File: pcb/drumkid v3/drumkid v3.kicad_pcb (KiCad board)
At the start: 2 copper layers, 90 x 120 mm, 61 parts, among them J1 Conn_01x04_Female, J5 Conn_01x05_Female, J6 Conn_01x04_Female, J7 Conn_01x06_Female, J8 Conn_01x05_Female, J9 AudioJack3_Ground_Switch, SW1 SW_SPDT, SW2 SW_Push, SW3 SW_Push, SW4 SW_Push, SW5 SW_Push, SW6 SW_Push, SW7 SW_Push, U2 ATmega328P-PU, U3 LM386, Y1 Crystal

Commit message: pcb layout looking nice (v3)
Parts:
- moved C16 16.9 mm to (167.7, 130.8)
- moved R8 10.4 mm to (142.2, 124.6), turned to 90 degrees
- moved R9 9.22 mm to (137.2, 124.6), turned to 90 degrees
- moved R1 8.99 mm to (139.7, 124.6), turned to 90 degrees
- moved R2 7.71 mm to (174.0, 133.3)
- moved R7 5.28 mm to (174.0, 130.8)
- moved R6 4.83 mm to (174.0, 128.3)
- moved U2 4.74 mm to (172.7, 139.7)
- moved R5 4.38 mm to (174.0, 125.7)
- moved R4 3.93 mm to (174.0, 123.2)
- moved R3 3.49 mm to (174.0, 120.7)
- moved J1 3.43 mm to (125.7, 146.1)
- moved C14 2.36 mm to (128.3, 134.6)
- moved C18 2.29 mm to (167.6, 125.7)
- moved C15 2.28 mm to (128.3, 118.1)
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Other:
- board text added: "5V 5V GND GND"
- board text added: "D4 D3 D2 D1 D0 A5 A4 A3 A2 A1 A0"
- board text added: "D5 D6 D7 D8 D9 D10 D11 D12 D13"

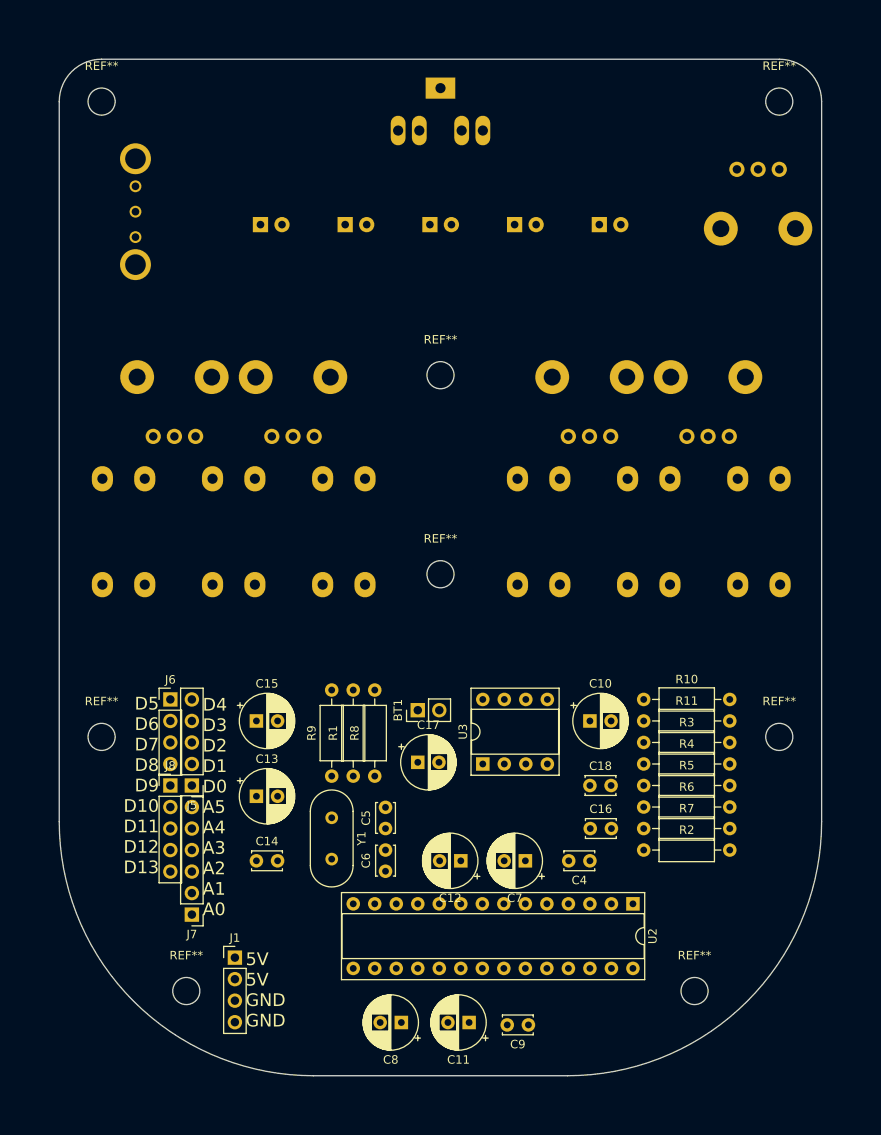
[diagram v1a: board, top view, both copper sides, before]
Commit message: silkscreen layers looking decent
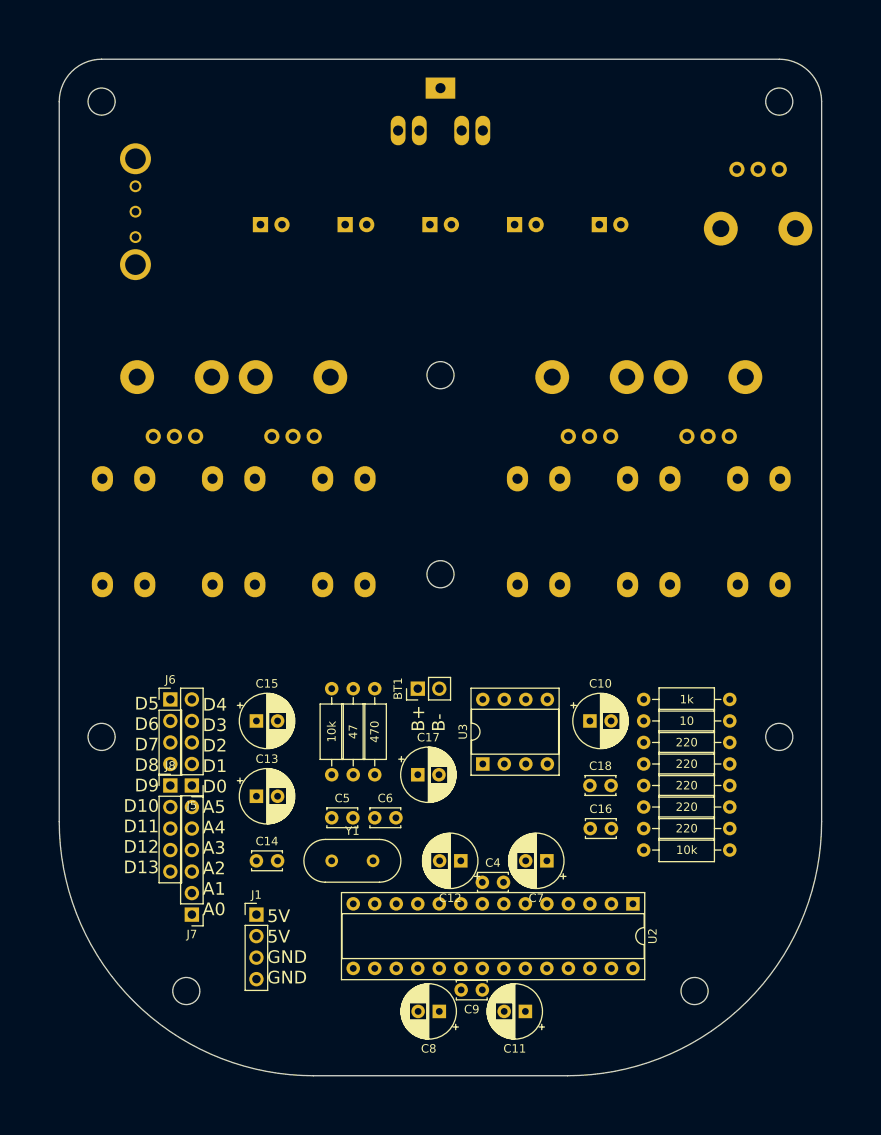
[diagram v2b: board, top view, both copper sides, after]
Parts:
- D2, D3, D4, D5, D6: footprint LED_THT:LED_D5.0mm -> headphone:LED_D5.0mm_NOSILK
- J9: footprint headphone:Tayda_3.5mm_stereo_TRS_jack_A-853 -> headphone:Tayda_3.5mm_stereo_TRS_jack_A-853_NOSILK
- R1, R10, R11, R2, R3, R4, R5, R6, R7, R8, R9: footprint Resistor_THT:R_Axial_DIN0207_L6.3mm_D2.5mm_P10.16mm_Horizontal -> headphone:R_Axial_DIN0207_L6.3mm_D2.5mm_P10.16mm_Horizontal_VALMOD
- RV1, RV2, RV3, RV4, RV5: footprint Potentiometer_THT:Potentiometer_Alps_RK09K_Single_Vertical -> headphone:Potentiometer_Alps_RK09K_Single_Vertical_NOSILK
- SW1: footprint SamacSys_Parts:EG1206 -> headphone:EG1206_NOSILK
- SW2, SW3, SW4, SW5, SW6, SW7: footprint Button_Switch_THT:SW_PUSH-12mm_Wuerth-430476085716 -> headphone:SW_PUSH-12mm_Wuerth-430476085716_NOSILK
- moved C4 13.0 mm to (154.9, 137.2), turned to 0 degrees
- moved C9 6.83 mm to (154.9, 149.9)
- moved C11 6.77 mm to (160.0, 152.4)
- moved C5 6.48 mm to (137.2, 129.5), turned to 0 degrees
- moved C6 6.44 mm to (142.2, 129.5), turned to 0 degrees
- moved J1 5.68 mm to (128.3, 141.0)
- moved Y1 5.08 mm to (137.2, 134.6), turned to 0 degrees
- moved C8 4.67 mm to (149.9, 152.4)
- moved BT1 2.54 mm to (147.3, 114.3)
- moved C7 2.54 mm to (162.6, 134.6)
- moved C17 1.47 mm to (147.3, 124.5)
- moved R1 0.16 mm to (139.7, 124.5)
- moved R8 0.16 mm to (142.2, 124.5)
- moved R9 0.16 mm to (137.2, 124.5)
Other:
- board text added: "B+ B-"

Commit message: half way through routing
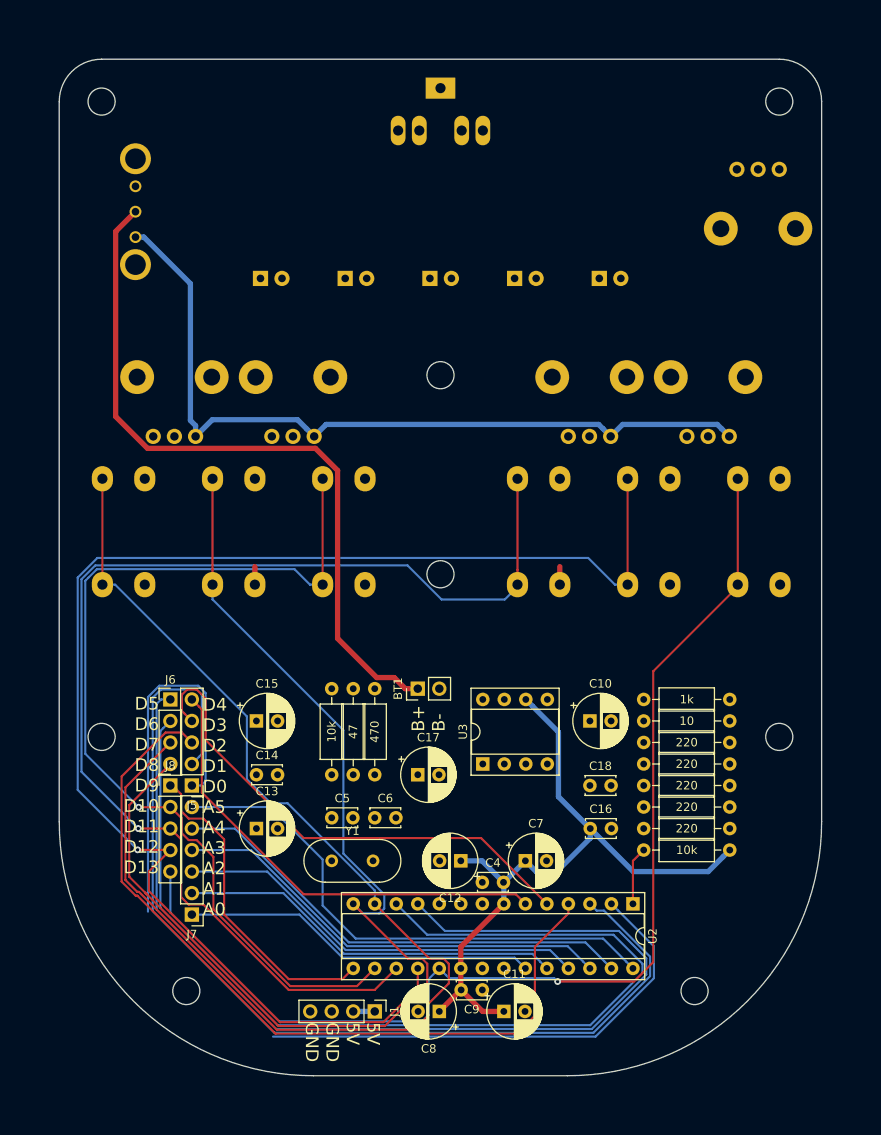
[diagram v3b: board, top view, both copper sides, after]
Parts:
- moved J1 18.1 mm to (142.2, 152.4), turned to 270 degrees
- moved C14 10.2 mm to (128.3, 124.5)
- moved D2 6.35 mm to (128.8, 65.9)
- moved D3 6.35 mm to (138.8, 65.9)
- moved D4 6.35 mm to (148.8, 65.9)
- moved D5 6.35 mm to (158.8, 65.9)
- moved D6 6.35 mm to (168.8, 65.9)
- moved C13 3.81 mm to (128.3, 130.8)
- moved C11 2.54 mm to (157.5, 152.4), turned to 0 degrees
- moved C7 2.54 mm to (160.0, 134.6), turned to 0 degrees
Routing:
- net +5V: track 0.00 -> 179.9 mm
- net /DIGITAL_12: track 0.00 -> 166.6 mm, vias 0 -> 1
- net /DIGITAL_7: track 0.00 -> 146.5 mm
- net /DIGITAL_11: track 0.00 -> 142.8 mm, vias 0 -> 1
- net /DIGITAL_8: track 0.00 -> 137.7 mm
- net /DIGITAL_13: track 0.00 -> 135.0 mm, vias 0 -> 1
- net /DIGITAL_5: track 0.00 -> 124.0 mm
- net /DIGITAL_6: track 0.00 -> 120.8 mm
- net /DIGITAL_1: track 0.00 -> 119.7 mm
- net /DIGITAL_10: track 0.00 -> 113.3 mm, vias 0 -> 1
- net /DIGITAL_0: track 0.00 -> 104.0 mm
- net /DIGITAL_2: track 0.00 -> 95.3 mm
- net Net-(BT1-Pad1): track 0.00 -> 85.7 mm
- net /ANALOG_5: track 0.00 -> 63.1 mm
- net /DIGITAL_3: track 0.00 -> 60.3 mm
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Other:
- net class Chunky added: clearance 0.2, trace_width 0.625, via_dia 0.8, via_drill 0.4
- board text added: "drumkid"

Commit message: nearly done routing
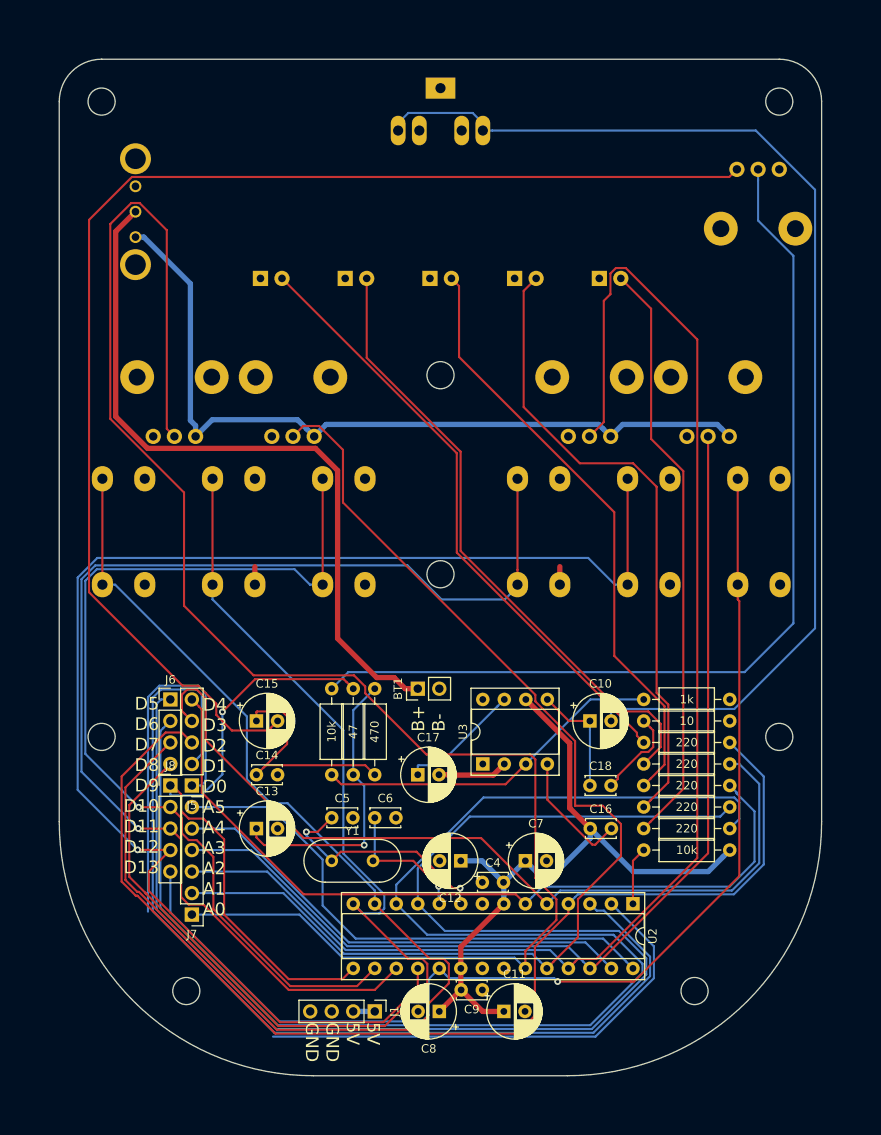
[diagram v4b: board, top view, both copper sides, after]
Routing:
- net /ANALOG_0: track 42.0 -> 201.1 mm
- net Net-(C15-Pad2): track 0.00 -> 153.2 mm
- net Net-(C10-Pad2): track 0.00 -> 135.9 mm
- net /ANALOG_2: track 49.2 -> 165.3 mm
- net Net-(R9-Pad2): track 0.00 -> 113.0 mm
- net /ANALOG_1: track 45.6 -> 133.5 mm
- net Net-(D5-Pad2): track 0.00 -> 75.0 mm
- net Net-(D3-Pad2): track 0.00 -> 74.4 mm
- net Net-(D2-Pad2): track 0.00 -> 72.5 mm
- net Net-(D4-Pad2): track 0.00 -> 71.3 mm
- net Net-(D6-Pad2): track 0.00 -> 69.9 mm
- net /ANALOG_3: track 52.8 -> 121.6 mm
- net /DIGITAL_6: track 120.8 -> 171.6 mm
- net /DIGITAL_5: track 124.0 -> 168.0 mm
- net Net-(R10-Pad1): track 0.00 -> 41.4 mm
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
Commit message: routing done! v3 send for fabrication...
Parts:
- moved BT1 41.3 mm to (177.8, 142.2)
- moved J1 21.6 mm to (125.7, 138.4), turned to 0 degrees
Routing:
- net GND: track 12.5 -> 143.8 mm, vias 0 -> 3
- net Net-(BT1-Pad1): track 85.7 -> 167.0 mm
- net +5V: track 179.9 -> 259.0 mm, vias 0 -> 1
- net /ANALOG_0: track 201.1 -> 143.8 mm
- net /DIGITAL_0: track 104.0 -> 124.8 mm
- net Net-(C15-Pad2): track 153.2 -> 139.5 mm
- net /DIGITAL_13: track 135.4 -> 140.9 mm
- net Net-(R9-Pad2): track 113.0 -> 116.9 mm
- net /ANALOG_1: track 133.5 -> 135.7 mm
- net /DIGITAL_7: track 146.5 -> 144.7 mm
- net /DIGITAL_12: track 166.6 -> 167.5 mm
- added copper zone on B.Cu, net GND
- added copper zone on F.Cu, net GND
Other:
- board text added: "DrumKid v03 by Matt Bradshaw mattbradshawdesign.com"
